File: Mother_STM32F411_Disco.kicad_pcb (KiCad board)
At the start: 2 copper layers, 234 x 114 mm, 29 parts, among them U1 ESP32-DEVKIT-V1

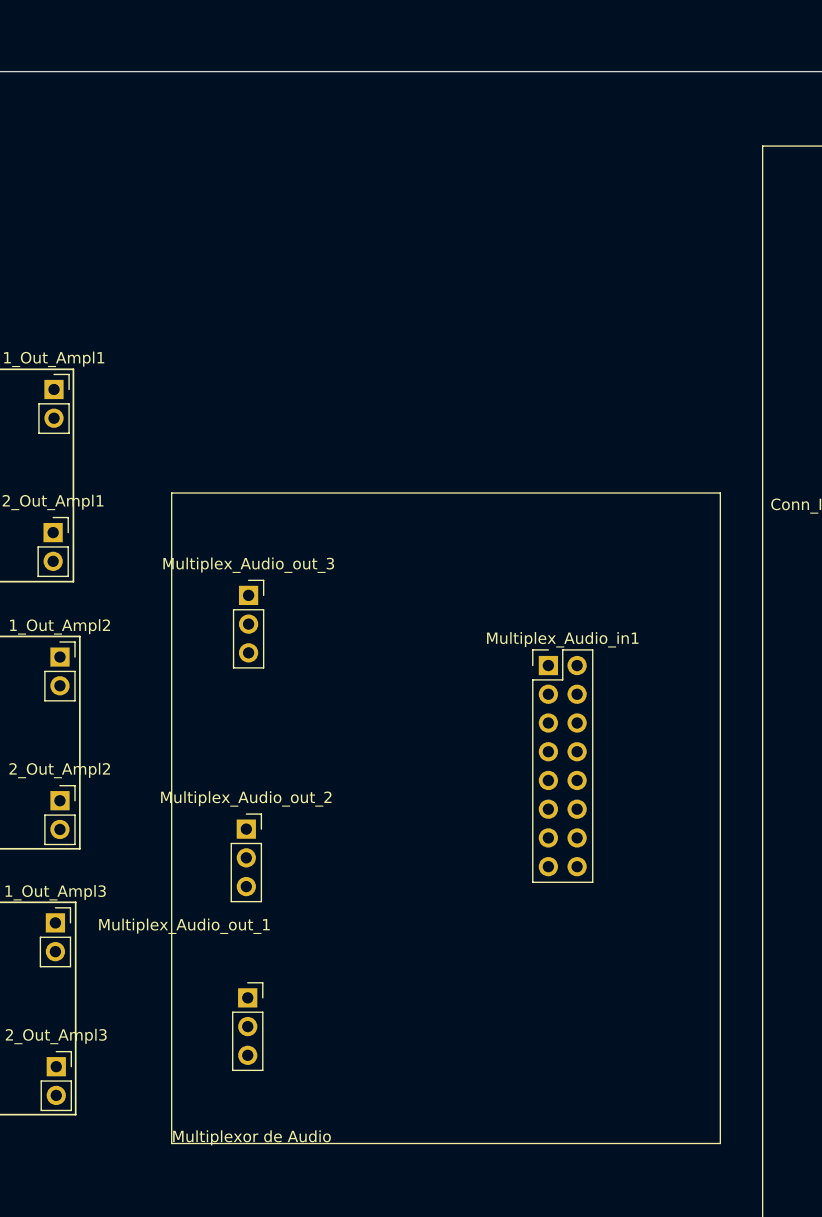
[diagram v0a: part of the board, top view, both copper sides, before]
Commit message: Huellas placas check, falta huellas filtros
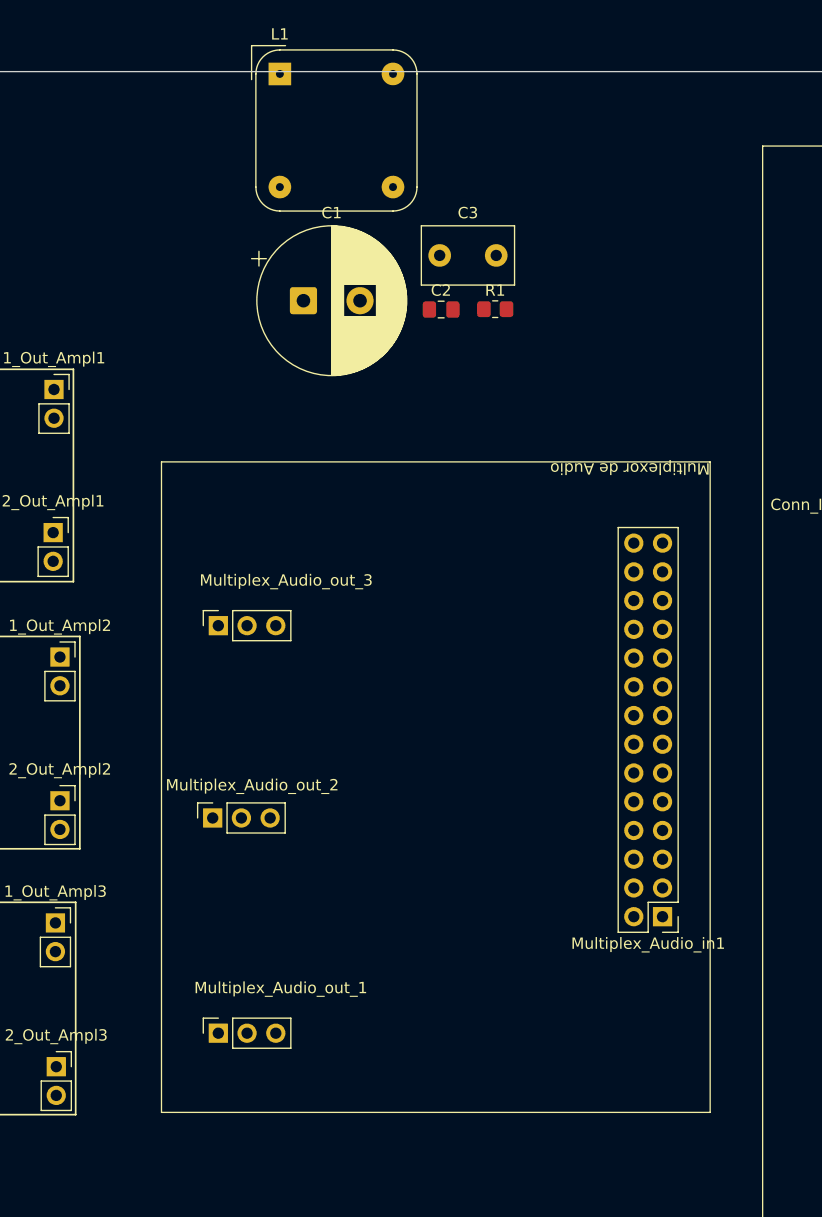
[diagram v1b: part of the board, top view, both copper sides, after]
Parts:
- added C1: C, Capacitor_THT:CP_Radial_D13.0mm_P5.00mm, F.Cu at (97.0, 56.2)
- added C2: C, Capacitor_SMD:C_0805_2012Metric_Pad1.18x1.45mm_HandSolder, F.Cu at (109.2, 57.0)
- added C3: C, Capacitor_THT:C_Disc_D8.0mm_W5.0mm_P5.00mm, F.Cu at (109.1, 52.2)
- added L1: L, Inductor_THT:Choke_Schaffner_RN102-04-14.0x14.0mm, F.Cu at (95.0, 36.2)
- added R1: R, Resistor_SMD:R_0805_2012Metric_Pad1.20x1.40mm_HandSolder, F.Cu at (114.0, 57.0)
- Multiplex_Audio_in1: footprint Connector_PinHeader_2.54mm:PinHeader_2x08_P2.54mm_Vertical -> Connector_PinHeader_2.54mm:PinHeader_2x14_P2.54mm_Vertical
- moved Multiplex_Audio_in1 24.4 mm to (128.8, 110.7), turned to 180 degrees
- moved Multiplex_Audio_out_1 4.07 mm to (89.5, 121.0), turned to 90 degrees
- moved Multiplex_Audio_out_3 3.78 mm to (89.5, 85.0), turned to 90 degrees
- moved Multiplex_Audio_out_2 3.13 mm to (89.0, 102.0), turned to 90 degrees
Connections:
- SRC_5V1 pad 1: unconnected-(SRC_5V1-Pin_1-Pad1) -> Net-(SRC_5V1-Pin_1)
- SRC_5V1 pad 2: unconnected-(SRC_5V1-Pin_2-Pad2) -> Net-(SRC_5V1-Pin_1)
- SRC_GND1 pad 1: unconnected-(SRC_GND1-Pin_1-Pad1) -> /GND
- SRC_GND1 pad 2: unconnected-(SRC_GND1-Pin_2-Pad2) -> /GND

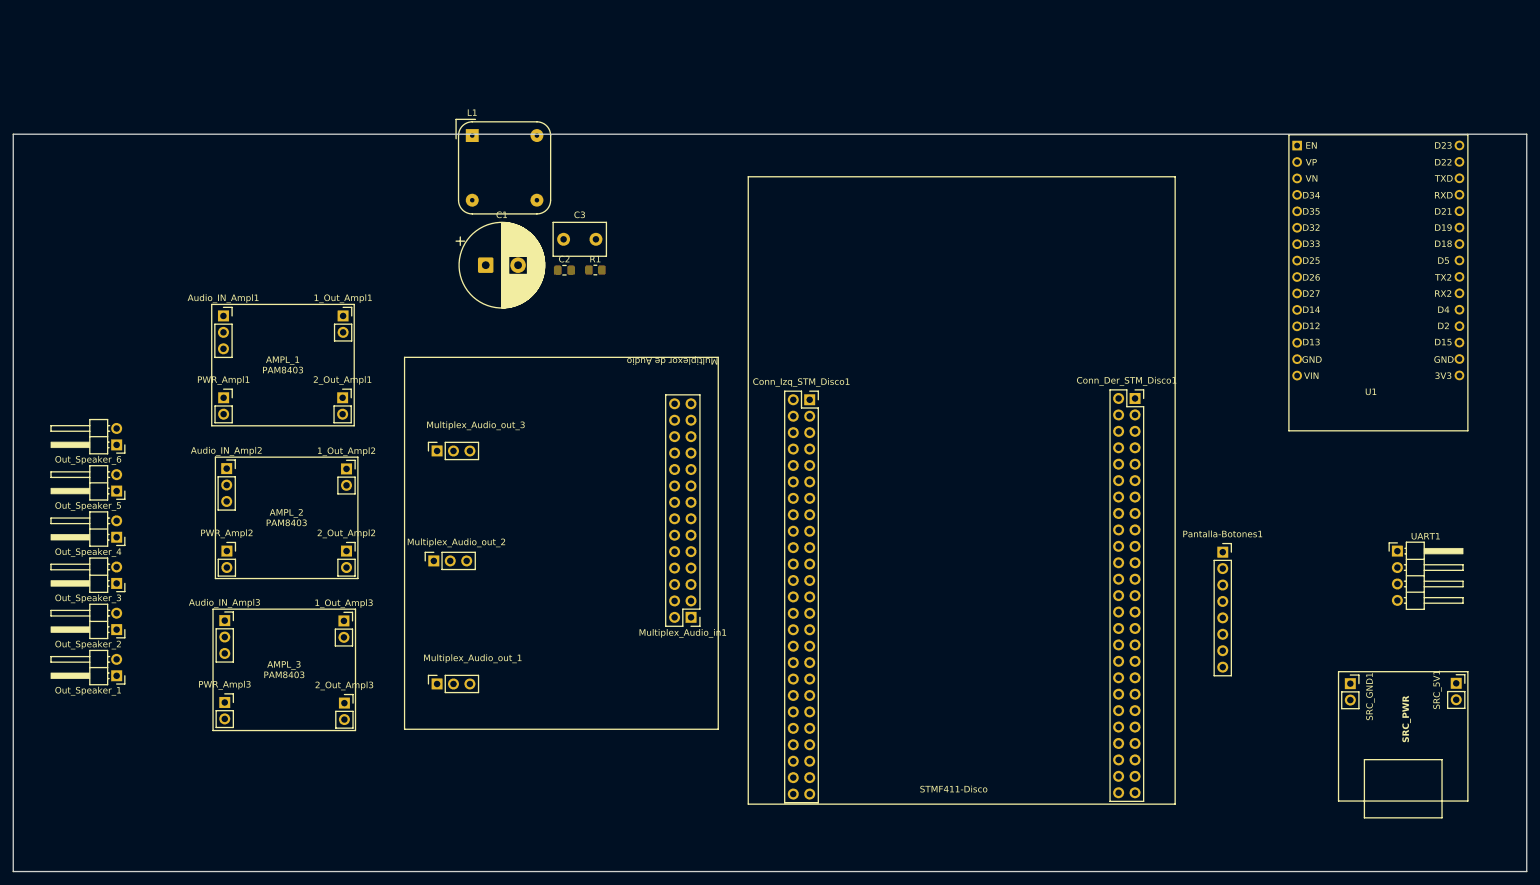
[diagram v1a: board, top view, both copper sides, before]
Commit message: fixed tamaño placa SRC_Supply
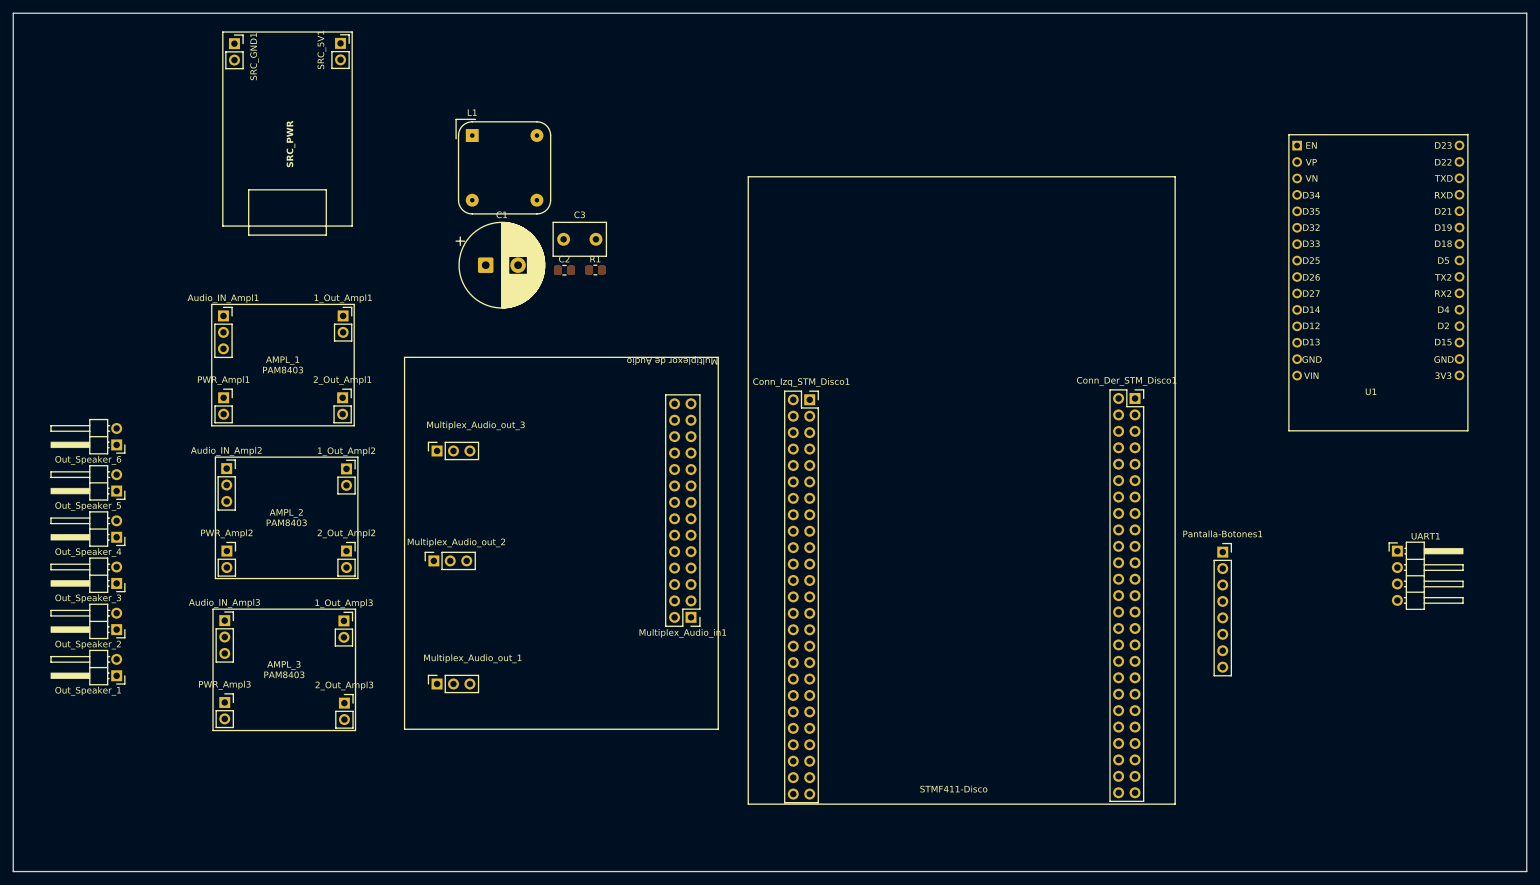
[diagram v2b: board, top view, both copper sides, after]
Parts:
- moved SRC_GND1 198.9 mm to (58.2, 22.0)
- moved SRC_5V1 198.9 mm to (74.6, 22.0)
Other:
- board size 234 x 114 mm -> 234 x 132.7 mm
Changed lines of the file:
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@@
 	(footprint "Connector_PinSocket_2.54mm:PinSocket_1x02_P2.54mm_Vertical"
 		(layer "F.Cu")
-		(at 230.725 120.95)
+		(at 58.2 22)
 		(descr "Through hole straight socket strip, 1x02, 2.54mm pitch, single row (from Kicad 4.0.7), script generated")
 		(tags "Through hole socket strip THT 1x02 2.54mm single row")
@@
 	(footprint "Connector_PinSocket_2.54mm:PinSocket_1x02_P2.54mm_Vertical"
 		(layer "F.Cu")
-		(at 247.1 120.9)
+		(at 74.6 21.96)
 		(descr "Through hole straight socket strip, 1x02, 2.54mm pitch, single row (from Kicad 4.0.7), script generated")
 		(tags "Through hole socket strip THT 1x02 2.54mm single row")
@@
 	)
 	(gr_rect
-		(start 133 128)
-		(end 84.5 70.5)
+		(start 84.5 70.5)
+		(end 133 128)
 		(stroke
 			(width 0.1)
@@
 	)
 	(gr_rect
-		(start 228.9 119.1)
-		(end 248.9 139.1)
+		(start 56.4 20.2)
+		(end 76.4 50.2)
 		(stroke
 			(width 0.1)
@@
 	)
 	(gr_rect
-		(start 232.9 132.7)
-		(end 244.9 141.7)
+		(start 60.4 44.6)
+		(end 72.4 51.6)
 		(stroke
 			(width 0.1)
@@
 	)
 	(gr_rect
-		(start 24 36)
+		(start 24 17.3)
 		(end 258 150)
 		(stroke
@@
 	)
 	(gr_text "SRC_PWR"
-		(at 239.9 130.1 90)
+		(at 67.4 41.2 90)
 		(layer "F.SilkS")
 		(effects
@@
 	)
 	(group ""
-		(members "ab75421f-f85e-4ebc-a8bf-16c65ca046c3" "c0988d01-2bfa-422b-a9ad-11baa444b9d6"
-			"dbc78347-1f85-4cc7-9f12-62f500dda437" "e4d125d4-9604-458c-a96e-ff6ce812214a"
-		)
-	)
-	(group ""
 		(members "0eede9cc-b46e-4660-a250-7d040d62f4f9" "5e30e5a8-f5a7-4d18-bb9e-ca18e7603b57"
 			"926aa707-d353-4d9e-b247-3f0da4009267" "d530fea6-de63-4045-9893-a1a0002c3ecc"
@@
 	)
 	(group ""
-		(members "5ce35fcc-e7d7-4282-bcb4-78cb0d50fe2c" "f276820b-dca7-44df-9834-89fc6e7dc30e")
+		(members "ab75421f-f85e-4ebc-a8bf-16c65ca046c3" "c0988d01-2bfa-422b-a9ad-11baa444b9d6"
+			"dbc78347-1f85-4cc7-9f12-62f500dda437" "e4d125d4-9604-458c-a96e-ff6ce812214a"
+			"f276820b-dca7-44df-9834-89fc6e7dc30e"
+		)
 	)
 	(group ""
